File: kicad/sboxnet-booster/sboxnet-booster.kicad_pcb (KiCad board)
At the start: 2 copper layers, 70 parts, among them J1 sboxnet-stecker_02x17, J3 Conn_01x02_Male, J4 Conn_01x02_Male, J5 Screw_Terminal_01x04, J6 Screw_Terminal_01x04, J7 Power von externen 15V/4A Net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, SW1 Öffner, U1 L6206PSO-sboxnet, U2 L78L12_SOT89

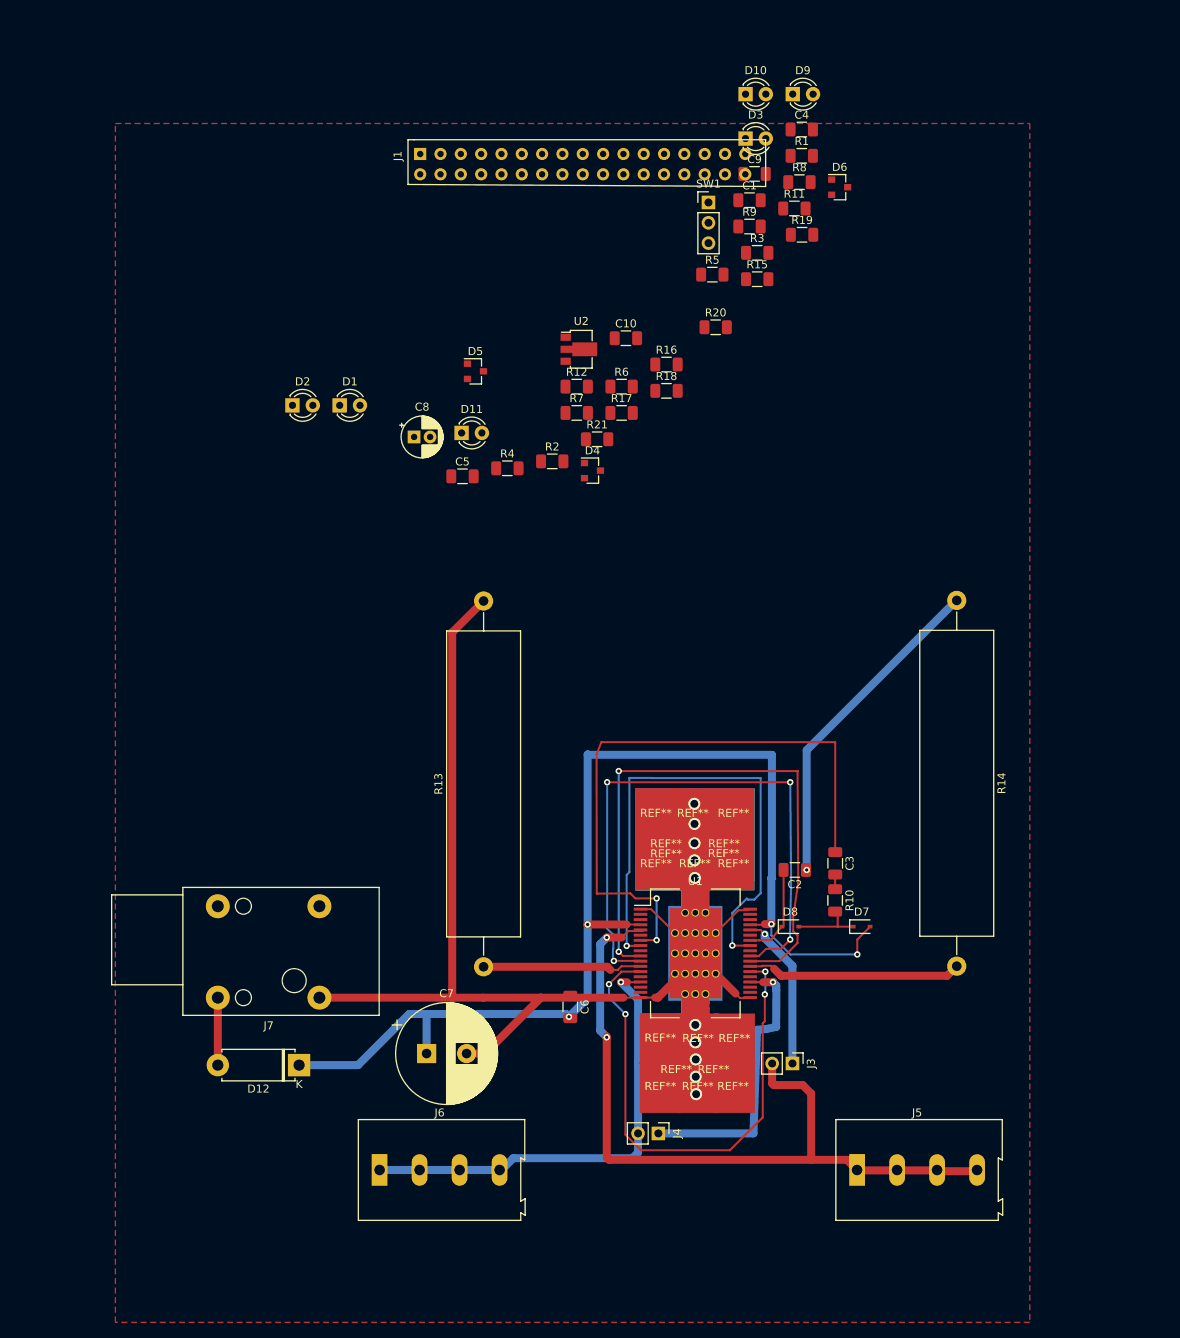
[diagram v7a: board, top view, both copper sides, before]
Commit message: layout LEDs
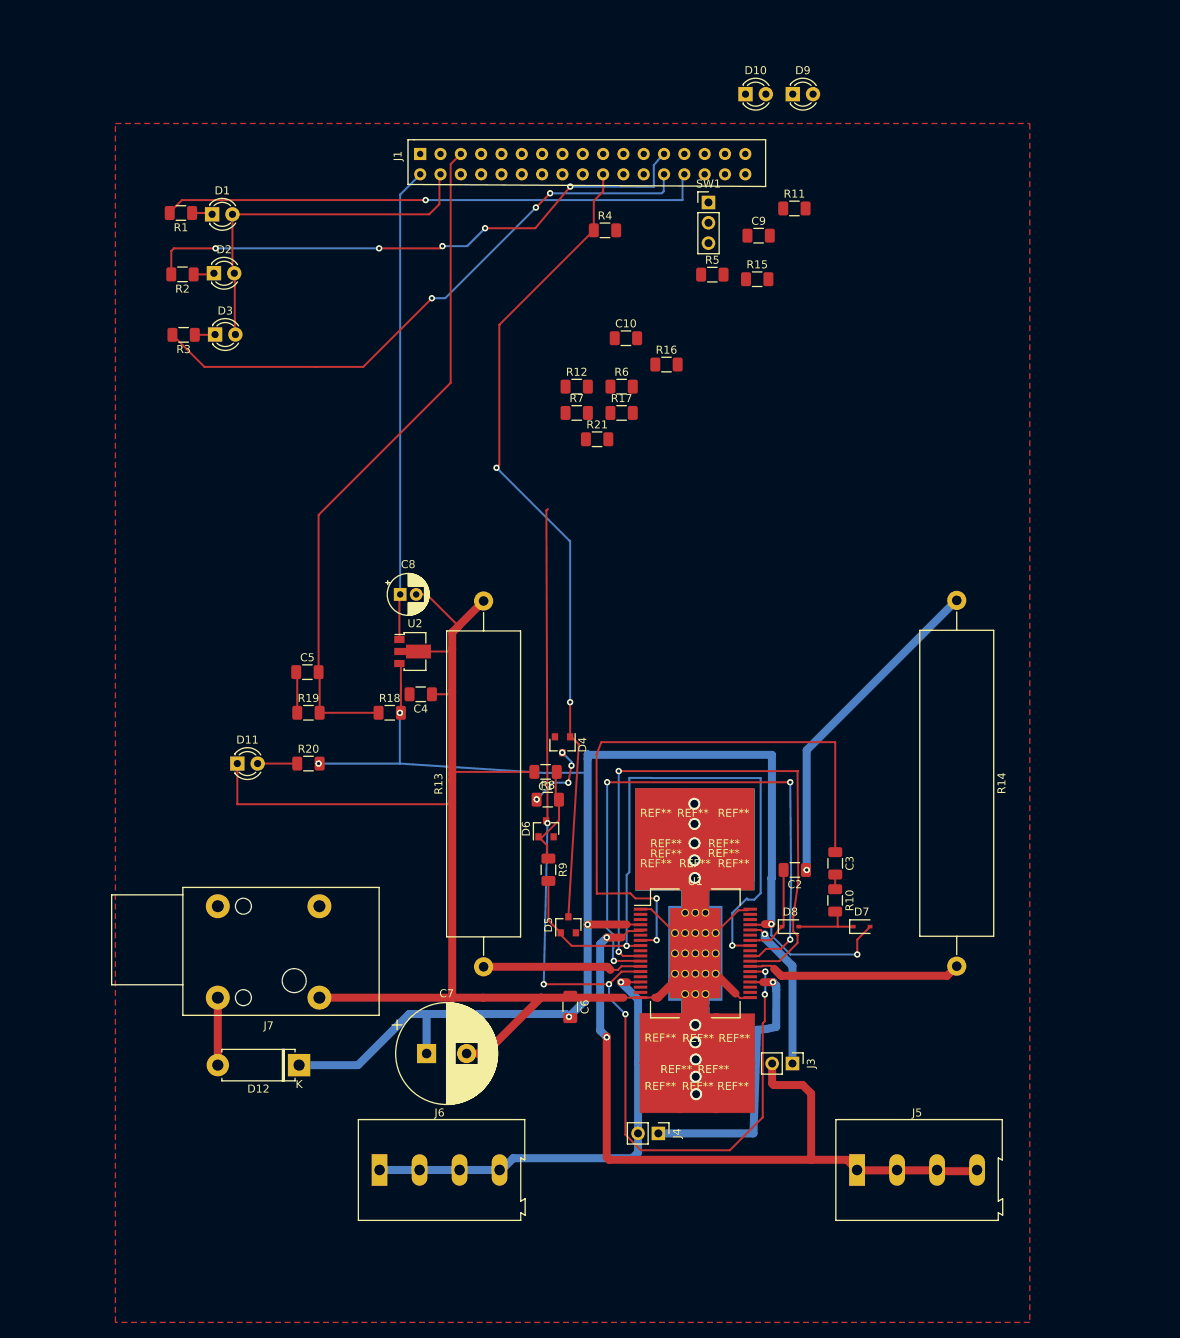
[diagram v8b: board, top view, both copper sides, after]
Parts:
- moved D6 88.2 mm to (79.2, 113.6), turned to 90 degrees
- moved R19 85.9 mm to (49.5, 99.1)
- moved C4 85.2 mm to (63.6, 96.7), turned to 180 degrees
- moved R9 84.2 mm to (79.5, 118.7), turned to 270 degrees
- moved R8 83.3 mm to (79.5, 109.9)
- moved R1 77.9 mm to (33.6, 36.6), turned to 180 degrees
- moved C1 75.9 mm to (79.2, 106.5), turned to 180 degrees
- moved R20 74.6 mm to (49.5, 105.4)
- moved R3 72.4 mm to (33.9, 51.8), turned to 180 degrees
- moved D3 70.7 mm to (37.9, 51.8)
- moved D5 70.2 mm to (82.0, 125.6), turned to 90 degrees
- moved R18 53.1 mm to (59.7, 99.1)
- moved R2 51.8 mm to (33.8, 44.3), turned to 180 degrees
- moved D11 49.9 mm to (40.6, 105.4)
- moved U2 43.1 mm to (62.5, 91.4)
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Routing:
- net PC2: track 0.00 -> 102.7 mm, vias 0 -> 2
- net PA1: track 0.00 -> 84.8 mm
- net PD0: track 0.00 -> 74.2 mm, vias 0 -> 3
- net PD1: track 0.00 -> 71.4 mm, vias 0 -> 5
- net PD2: track 0.00 -> 68.1 mm, vias 0 -> 1
- net PC3: track 64.2 -> 131.9 mm, vias 4 -> 6
- net GND: track 211.7 -> 275.2 mm
- net +12V: track 0.00 -> 58.9 mm
- net V: track 146.1 -> 193.1 mm, vias 4 -> 6
- net +3V3: track 0.00 -> 44.9 mm
- net EN: track 64.7 -> 80.9 mm
- net Net-(C1-Pad1): track 0.00 -> 12.5 mm
- net Net-(D4-Pad3): track 0.00 -> 9.14 mm, vias 0 -> 4
- net Net-(D11-Pad2): track 0.00 -> 5.08 mm
- net Net-(D2-Pad1): track 0.00 -> 2.71 mm
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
